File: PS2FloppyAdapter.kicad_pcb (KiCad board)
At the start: 2 copper layers, 59.7 x 23.7 mm, 8 parts, among them J1 Conn_02x20_Odd_Even, J2 Conn_02x17_Odd_Even, J3 Conn_01x04

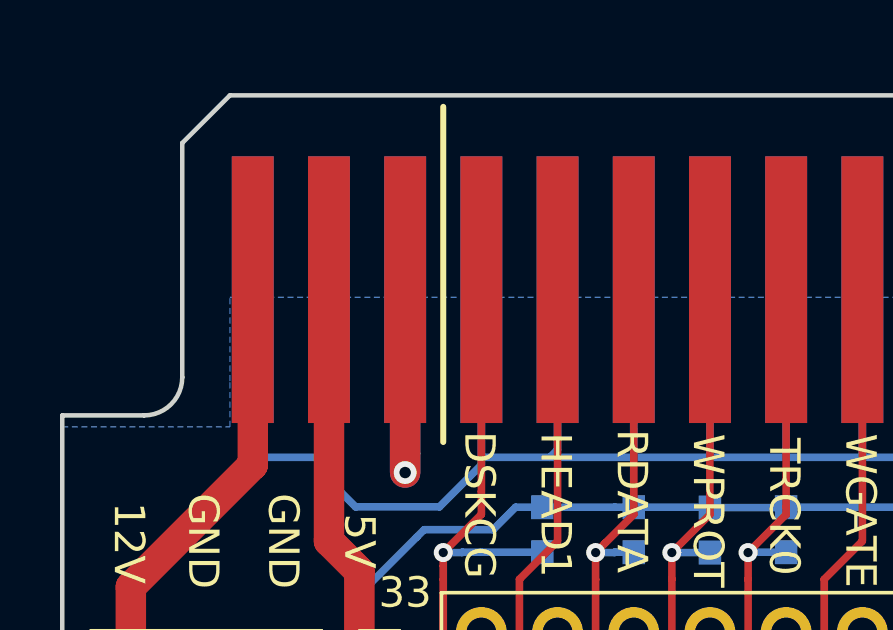
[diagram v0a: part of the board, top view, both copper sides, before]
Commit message: Add slot cutout
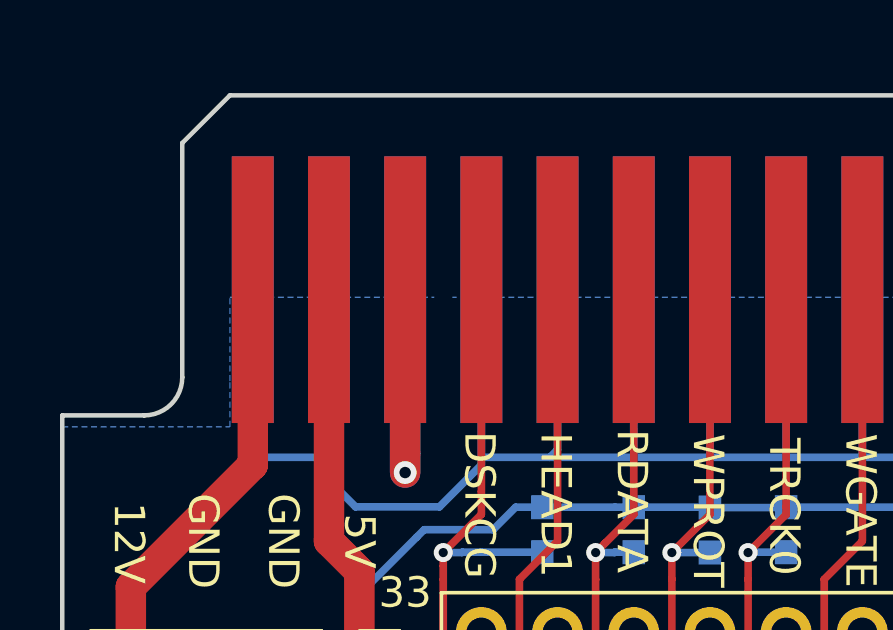
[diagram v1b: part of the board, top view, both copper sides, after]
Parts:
- added REF**: Slot_0_6mm, MountingHole:MountingHole_2.1mm, F.Cu at (138.7, 74.5)
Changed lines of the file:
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@@
-(kicad_pcb (version 20171130) (host pcbnew "(5.1.0)-1")
+(kicad_pcb (version 20171130) (host pcbnew 5.1.5-52549c5~84~ubuntu18.04.1)
   (general
     (thickness 1.6)
@@
     (tracks 171)
     (zones 0)
-    (modules 8)
+    (modules 9)
     (nets 22)
   )
@@
     (mod_text_size 1 1)
     (mod_text_width 0.15)
-    (pad_size 1.524 1.524)
-    (pad_drill 0.762)
+    (pad_size 0.6 13)
+    (pad_drill 0.6)
     (pad_to_mask_clearance 0.2)
     (aux_axis_origin 0 0)
@@
     (add_net "Net-(J1-Pad35)")
   )
+  (module MountingHole:MountingHole_2.1mm (layer F.Cu)
+    (at 138.684 74.4855)
+    (descr "Mounting Hole 2.1mm, no annular")
+    (tags "mounting hole 2.1mm no annular")
+    (attr virtual)
+    (fp_text reference REF** (at -1.524 7.7343) (layer F.SilkS) hide
+      (effects (font (size 0.1 0.1) (thickness 0.02)))
+    )
+    (fp_text value Slot_0_6mm (at 0 3.2) (layer F.Fab)
+      (effects (font (size 1 1) (thickness 0.15)))
+    )
+    (pad "" np_thru_hole roundrect (at -1.524 11.9888) (size 0.6 13) (drill oval 0.6 13) (layers *.Cu *.Mask) (roundrect_rratio 0.25))
+  )
   (module Conn:EDGE_FLOPPY40 (layer F.Cu)
     (at 154.94 87.63)
@@
   (gr_line (start 184.15 91.821) (end 184.15 103.632) (layer Edge.Cuts) (width 0.15))
   (gr_line (start 182.6895 91.821) (end 184.15 91.821) (layer Edge.Cuts) (width 0.15))
-  (gr_line (start 137.16 81.534) (end 137.16 92.71) (layer F.SilkS) (width 0.2))
+  (gr_line (start 137.16 81.534) (end 137.16 92.71) (layer F.Fab) (width 0.2))
   (gr_line (start 128.4605 90.551) (end 128.4605 82.7405) (layer Edge.Cuts) (width 0.15))
   (gr_line (start 181.4195 82.6135) (end 181.4195 90.551) (layer Edge.Cuts) (width 0.15))
